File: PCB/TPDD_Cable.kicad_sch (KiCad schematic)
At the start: 11 parts, among them J2 TPDD, P2 RX, P20 DSR, P3 TX, P4 CTS, P5 RTS, P6 DTR, P7 GND, Q1 DTA114EKA, Q2 DTA114EKA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

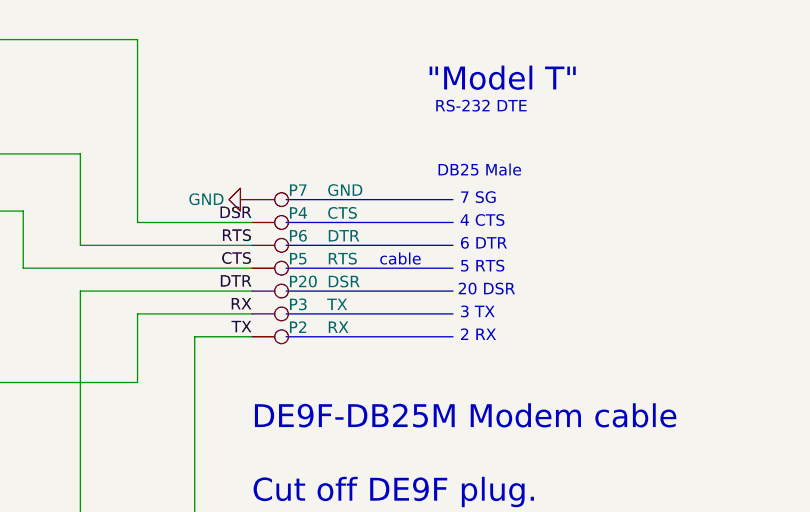
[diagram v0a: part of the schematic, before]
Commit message: housing: 0.8mm min-wall & many small fixes. pcb: pull in v1 & v2 pcbs from master & fancy2
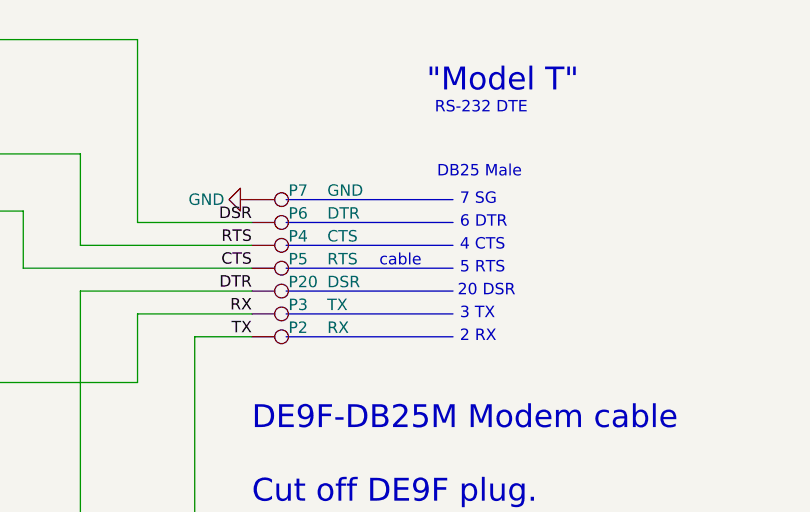
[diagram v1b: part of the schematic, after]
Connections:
- net DSR: now also P6.1; no longer P4.1
- net RTS: now also P4.1; no longer P6.1
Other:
- moved on the sheet: P4, P6
